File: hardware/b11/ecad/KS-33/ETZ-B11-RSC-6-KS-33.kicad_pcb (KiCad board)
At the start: 2 copper layers, 131.5 x 85.8 mm, 0 parts

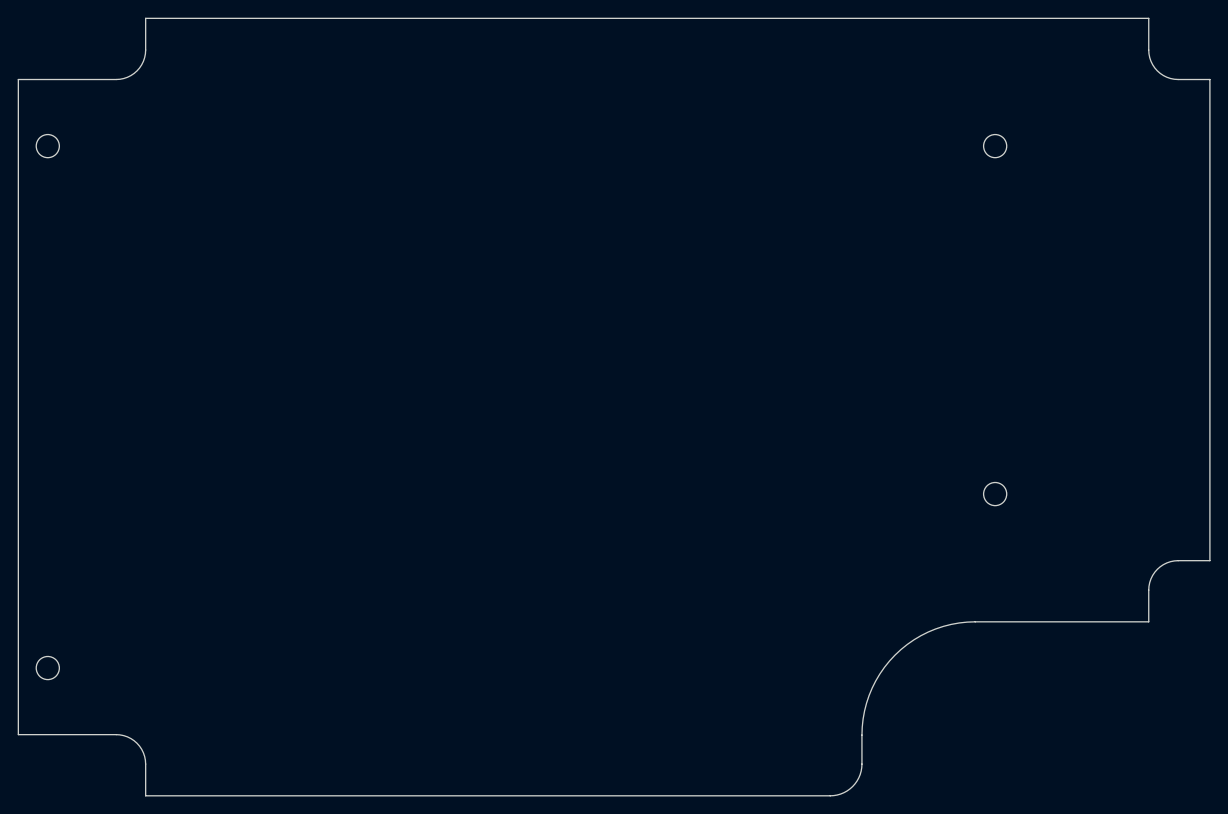
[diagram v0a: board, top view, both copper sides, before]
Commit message: fix(hardware/b11): fix 3D model paths, .kicad_pro files, KS-33 placement
- Update footprint model paths to \${KIPRJMOD}/../../../../lib/3d-models/
  so 3D models resolve correctly from ecad/{family}/ project directories
- Generate .kicad_pro for all 24 boards; remove dangling old ecad/ root .kicad_pro files
- Fix place-switch-sockets.py and place-switch-leds.py to read grid origin
  from board design settings instead of config constants
- Place KS-33 switch sockets and LEDs on all 4 carrier boards
- Propagate KiCad-normalised 1.6mm stackup across KS-33 SC boards

Co-Authored-By: Claude Sonnet 4.6 <noreply@anthropic.com>
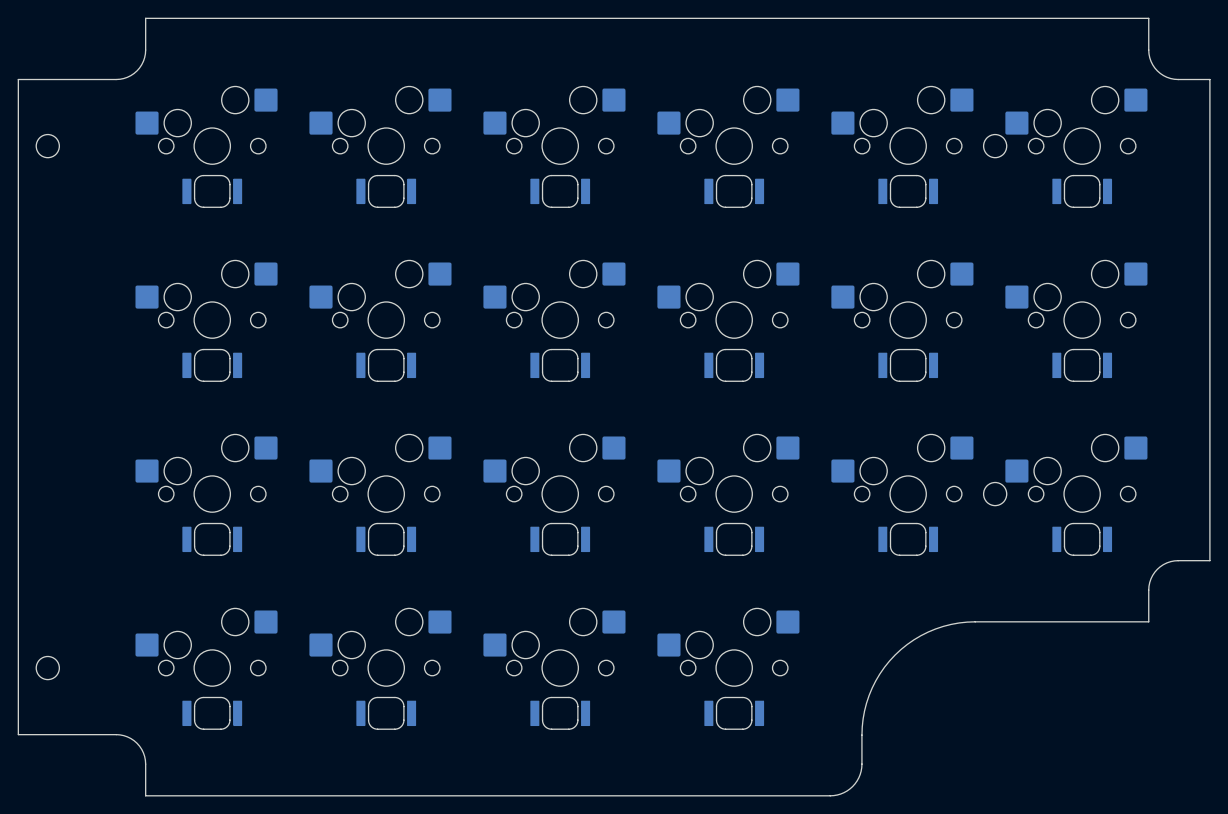
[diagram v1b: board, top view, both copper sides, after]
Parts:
- added LED1: 6028_LED, 6028_LED, F.Cu at (200.2, 78.3)
- added LED10: 6028_LED, 6028_LED, F.Cu at (142.6, 97.5)
- added LED11: 6028_LED, 6028_LED, F.Cu at (123.3, 97.5)
- added LED12: 6028_LED, 6028_LED, F.Cu at (104.2, 97.5)
- added LED13: 6028_LED, 6028_LED, F.Cu at (200.2, 116.7)
- added LED14: 6028_LED, 6028_LED, F.Cu at (180.9, 116.7)
- added LED15: 6028_LED, 6028_LED, F.Cu at (161.8, 116.7)
- added LED16: 6028_LED, 6028_LED, F.Cu at (142.6, 116.7)
- added LED17: 6028_LED, 6028_LED, F.Cu at (123.3, 116.7)
- added LED18: 6028_LED, 6028_LED, F.Cu at (104.2, 116.7)
- added LED19: 6028_LED, 6028_LED, F.Cu at (161.8, 135.9)
- added LED2: 6028_LED, 6028_LED, F.Cu at (180.9, 78.3)
- added LED20: 6028_LED, 6028_LED, F.Cu at (142.6, 135.9)
- added LED21: 6028_LED, 6028_LED, F.Cu at (123.3, 135.9)
- added LED22: 6028_LED, 6028_LED, F.Cu at (104.2, 135.9)
- added LED3: 6028_LED, 6028_LED, F.Cu at (161.8, 78.3)
- added LED4: 6028_LED, 6028_LED, F.Cu at (142.6, 78.3)
- added LED5: 6028_LED, 6028_LED, F.Cu at (123.3, 78.3)
- added LED6: 6028_LED, 6028_LED, F.Cu at (104.2, 78.3)
- added LED7: 6028_LED, 6028_LED, F.Cu at (200.2, 97.5)
- added LED8: 6028_LED, 6028_LED, F.Cu at (180.9, 97.5)
- added LED9: 6028_LED, 6028_LED, F.Cu at (161.8, 97.5)
- added SW1: KS-2P02B01-01-a, KS-2P02B01-01-a, F.Cu at (200.2, 73.3)
- added SW10: KS-2P02B01-01-a, KS-2P02B01-01-a, F.Cu at (142.6, 92.5)
- added SW11: KS-2P02B01-01-a, KS-2P02B01-01-a, F.Cu at (123.3, 92.5)
- added SW12: KS-2P02B01-01-a, KS-2P02B01-01-a, F.Cu at (104.2, 92.5)
- added SW13: KS-2P02B01-01-a, KS-2P02B01-01-a, F.Cu at (200.2, 111.7)
- added SW14: KS-2P02B01-01-a, KS-2P02B01-01-a, F.Cu at (180.9, 111.7)
- added SW15: KS-2P02B01-01-a, KS-2P02B01-01-a, F.Cu at (161.8, 111.7)
- added SW16: KS-2P02B01-01-a, KS-2P02B01-01-a, F.Cu at (142.6, 111.7)
- added SW17: KS-2P02B01-01-a, KS-2P02B01-01-a, F.Cu at (123.3, 111.7)
- added SW18: KS-2P02B01-01-a, KS-2P02B01-01-a, F.Cu at (104.2, 111.7)
- added SW19: KS-2P02B01-01-a, KS-2P02B01-01-a, F.Cu at (161.8, 130.9)
- added SW2: KS-2P02B01-01-a, KS-2P02B01-01-a, F.Cu at (180.9, 73.3)
- added SW20: KS-2P02B01-01-a, KS-2P02B01-01-a, F.Cu at (142.6, 130.9)
- added SW21: KS-2P02B01-01-a, KS-2P02B01-01-a, F.Cu at (123.3, 130.9)
- added SW22: KS-2P02B01-01-a, KS-2P02B01-01-a, F.Cu at (104.2, 130.9)
- added SW3: KS-2P02B01-01-a, KS-2P02B01-01-a, F.Cu at (161.8, 73.3)
- added SW4: KS-2P02B01-01-a, KS-2P02B01-01-a, F.Cu at (142.6, 73.3)
- added SW5: KS-2P02B01-01-a, KS-2P02B01-01-a, F.Cu at (123.3, 73.3)
- added SW6: KS-2P02B01-01-a, KS-2P02B01-01-a, F.Cu at (104.2, 73.3)
- added SW7: KS-2P02B01-01-a, KS-2P02B01-01-a, F.Cu at (200.2, 92.5)
- added SW8: KS-2P02B01-01-a, KS-2P02B01-01-a, F.Cu at (180.9, 92.5)
- added SW9: KS-2P02B01-01-a, KS-2P02B01-01-a, F.Cu at (161.8, 92.5)
